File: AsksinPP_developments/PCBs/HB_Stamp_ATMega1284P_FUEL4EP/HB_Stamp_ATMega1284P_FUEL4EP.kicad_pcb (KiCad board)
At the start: 2 copper layers, 22 x 40 mm, 39 parts, among them J1 Power, J2 FTDI Debuger, J3 ISP Programmer, J4 I2C, J5 PA5/PCINT5, J6 PB3/AIN1/PCINT11, J7 PC4/PCINT20, U1 ATmega1284P-AU, U2 TPS61221DCK

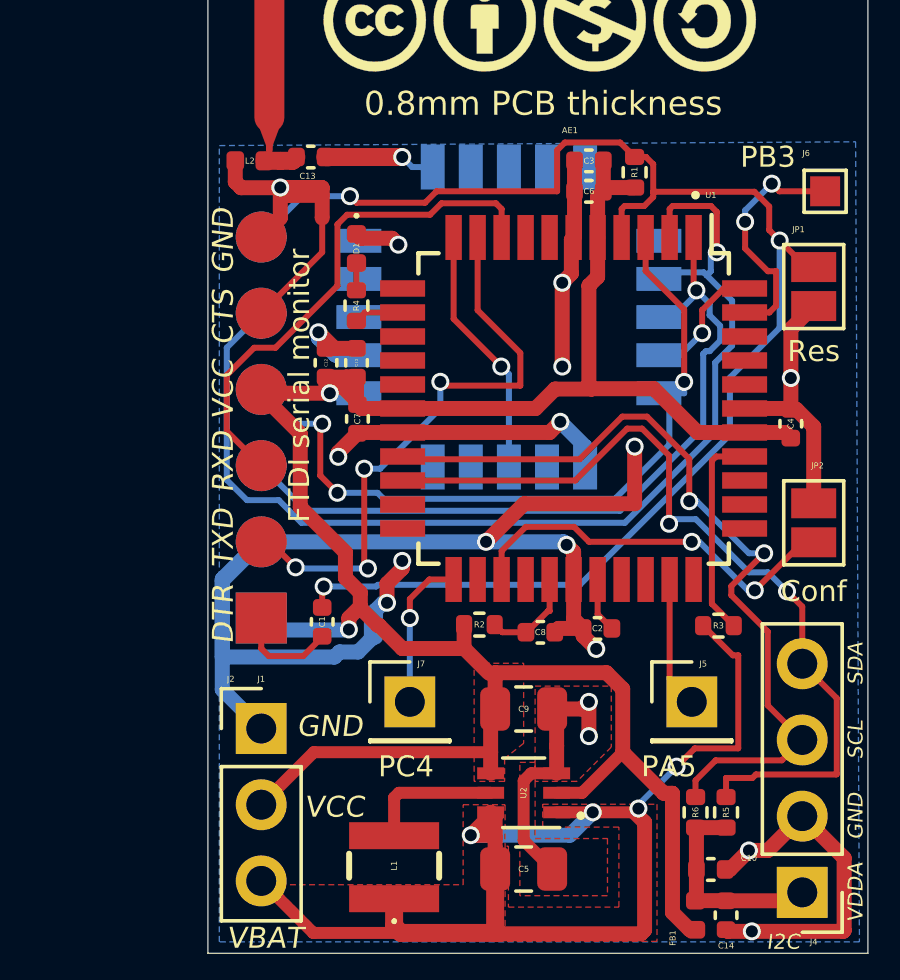
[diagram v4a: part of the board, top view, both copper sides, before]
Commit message: PCBs: HB_Stamp_ATMega1284P_FUEL4EP: Realized pads for pogo pin adapter as ring
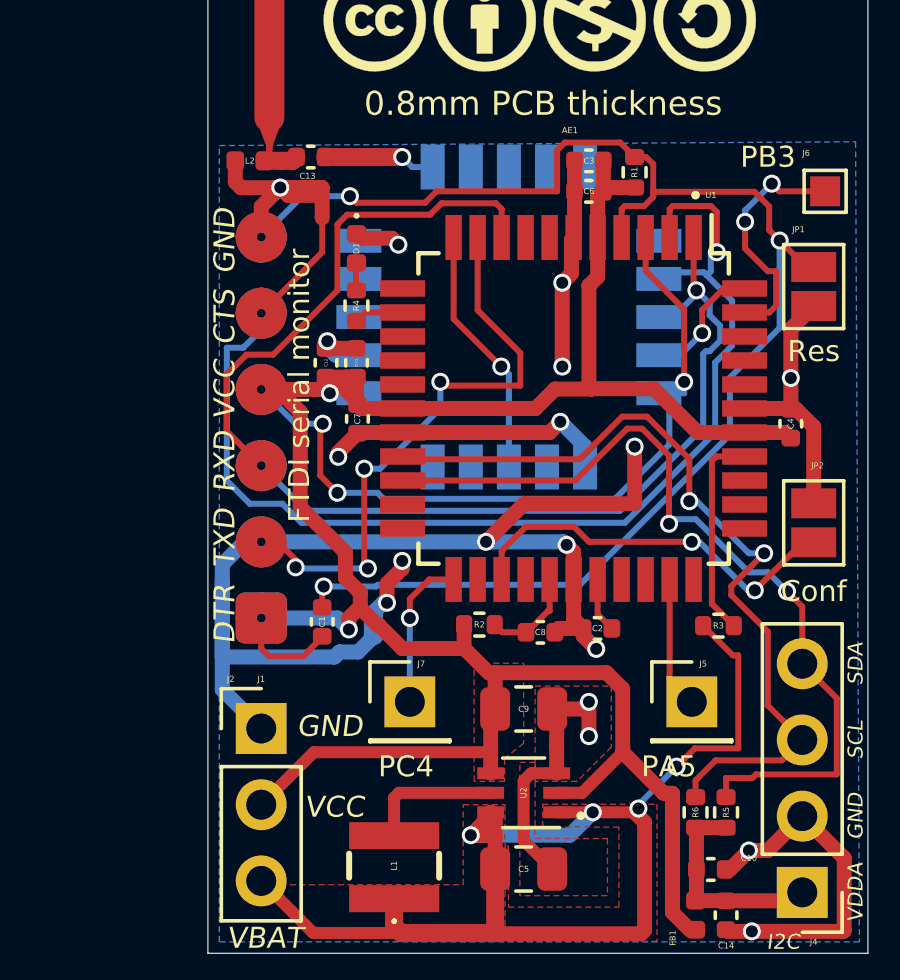
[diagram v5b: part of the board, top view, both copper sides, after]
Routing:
- net GND: track 102.8 -> 98.8 mm
- net VCC: track 78.3 -> 77.7 mm
- net /DTR: track 3.42 -> 2.87 mm
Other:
- board text added: "Version 1.4 - 02/2024 (KiCAD 6)"
- board text removed: "Version 1.3 - 02/2024 (KiCAD 6)"

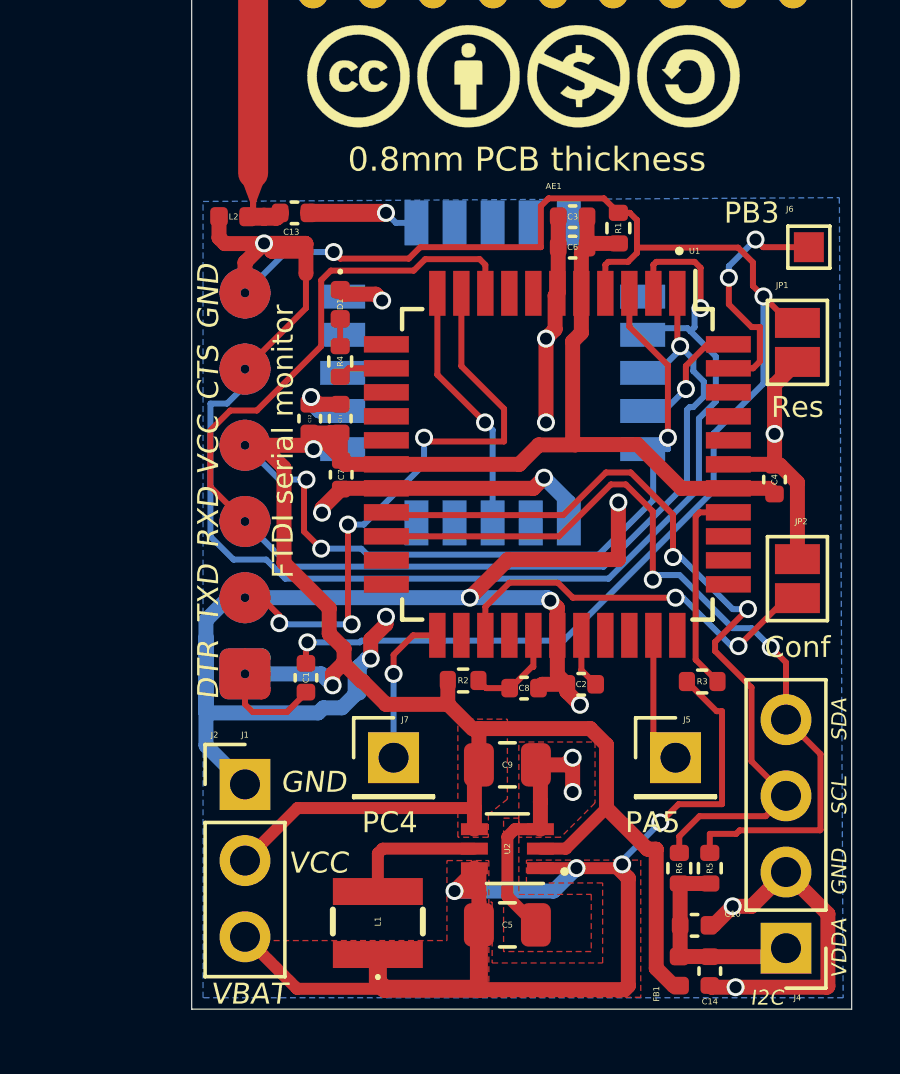
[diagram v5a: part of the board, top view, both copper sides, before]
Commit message: PCBs/HB_Stamp_ATMega1284P_FUEL4EP: migration to KiCAD 8
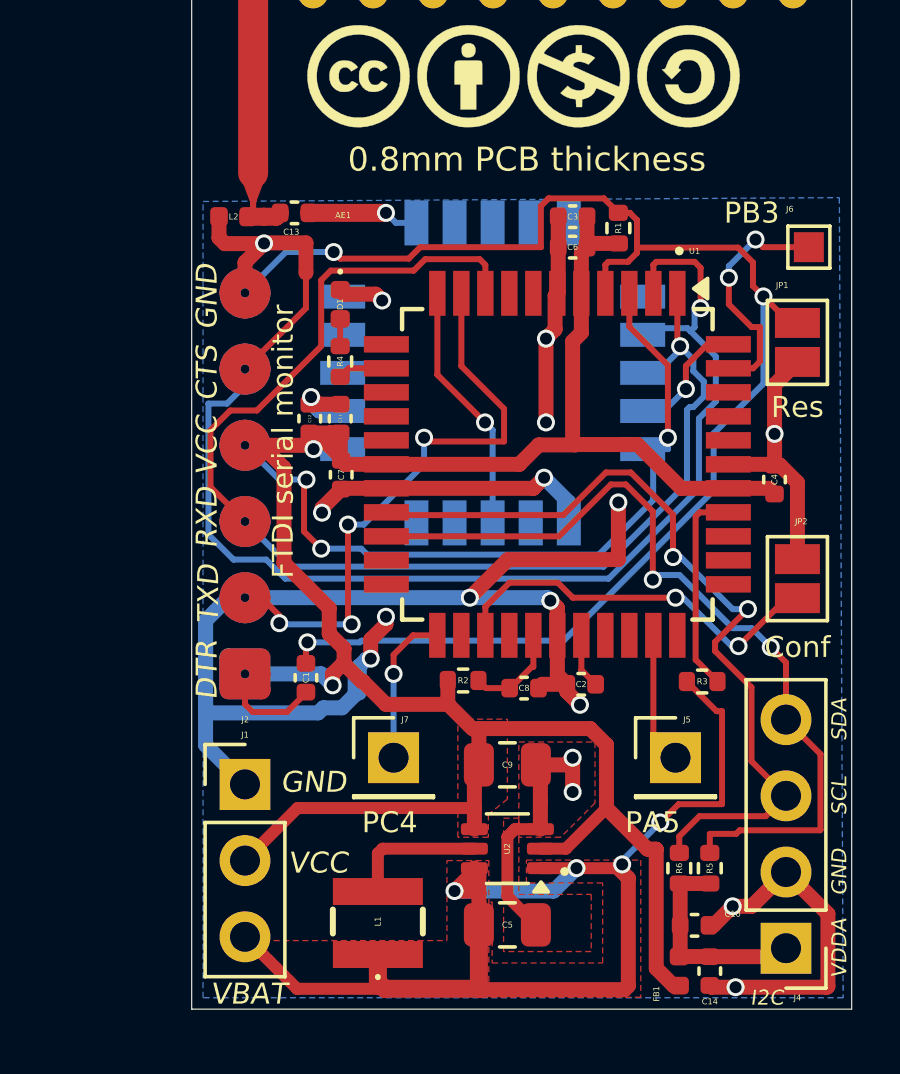
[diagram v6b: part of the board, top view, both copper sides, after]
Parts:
- AE1: footprint RF_Antenna:Texas_SWRA416_868MHz_915MHz -> FUEL4EP:Texas_SWRA416_868MHz_915MHz
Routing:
- net GND: track 98.8 -> 96.6 mm
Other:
- board text added: "868MHz SWRA416 antenna"
- board text added: "Version 1.5 - 09/2024 (KiCAD 8)"
- board text removed: "868MHz SWRA416 antrenna"
- board text removed: "Version 1.4 - 02/2024 (KiCAD 6)"

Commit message: PCBs: updated some JLCPCB manufacturing data after trial-order
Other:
- board text added: "JLCJLCJLCJLC"

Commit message: PCB updates
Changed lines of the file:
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@@
 		(attr smd)
 		(fp_line
-			(start -0.4 -1.5)
-			(end 0.4 -1.5)
+			(start -0.254 -1.524)
+			(end 0.254 -1.524)
 			(stroke
-				(width 0.2)
-				(type solid)
+				(width 0.12)
+				(type default)
 			)
 			(layer "F.SilkS")
@@
 		)
 		(fp_line
-			(start -0.4 1.5)
-			(end 0.4 1.5)
+			(start -0.254 1.524)
+			(end 0.254 1.524)
 			(stroke
-				(width 0.2)
-				(type solid)
+				(width 0.12)
+				(type default)
 			)
 			(layer "F.SilkS")
@@
 			)
 		)
-		(fp_text user "KEEP-OUT ZONE"
-			(at 1 -2.8 0)
+		(fp_text user "No metal, traces or "
+			(at 1 0.2 0)
 			(layer "Cmts.User")
 			(effects
@@
 			)
 		)
-		(fp_text user "No metal, traces or "
-			(at 1 0.2 0)
+		(fp_text user "KEEP-OUT ZONE"
+			(at 1 -2.8 0)
 			(layer "Cmts.User")
 			(effects
@@
 		(sheetfile "HB_Stamp_ATMega1284P_FUEL4EP.kicad_sch")
 		(zone_connect 1)
-		(attr exclude_from_pos_files exclude_from_bom)
+		(attr exclude_from_pos_files)
 		(fp_line
 			(start 1.4 -1)
@@
 		(sheetfile "HB_Stamp_ATMega1284P_FUEL4EP.kicad_sch")
 		(zone_connect 1)
-		(attr exclude_from_pos_files exclude_from_bom)
+		(attr exclude_from_pos_files)
 		(fp_line
 			(start 1.4 -1)
@@
 			)
 		)
-		(property "LCSC" "C3223181"
+		(property "LCSC" "C2043991"
 			(at 2.794 -52.832 0)
 			(layer "F.Fab")
@@
 			)
 		)
-		(property "Sim.Enable" ""
-			(at 0 0 180)
-			(unlocked yes)
-			(layer "F.Fab")
-			(hide yes)
-			(effects
-				(font
-					(size 1 1)
-					(thickness 0.15)
-				)
-			)
-		)
 		(property ki_fp_filters "Choke_* *Coil* Inductor_* L_*")
 		(sheetname "Stammblatt")
@@
 		(attr smd exclude_from_pos_files)
 		(fp_line
-			(start 0 -10)
-			(end 0 -8.02)
+			(start 0 -10.033)
+			(end 0 -8.255)
 			(stroke
 				(width 0.12)
-				(type solid)
+				(type default)
 			)
 			(layer "B.SilkS")
 		)
 		(fp_line
-			(start 0 -8.02)
-			(end 0.9 -8.02)
+			(start 0 -10.033)
+			(end 1.651 -10.033)
 			(stroke
 				(width 0.12)
-				(type solid)
+				(type default)
 			)
 			(layer "B.SilkS")
 		)
 		(fp_line
-			(start 0 -1.96)
-			(end 0 0)
+			(start 0 -8.255)
+			(end 1.016 -8.255)
 			(stroke
 				(width 0.12)
-				(type solid)
+				(type default)
 			)
 			(layer "B.SilkS")
@@
 		(fp_line
 			(start 0 0)
-			(end 1.98 0)
+			(end 0 -1.778)
 			(stroke
 				(width 0.12)
-				(type solid)
+				(type default)
 			)
 			(layer "B.SilkS")
 		)
 		(fp_line
-			(start 0.9 -8.02)
-			(end 0.9 -1.96)
+			(start 0 0)
+			(end 1.651 0)
 			(stroke
 				(width 0.12)
-				(type solid)
+				(type default)
 			)
 			(layer "B.SilkS")
 		)
 		(fp_line
-			(start 0.9 -1.96)
-			(end 0 -1.96)
+			(start 1.016 -8.255)
+			(end 1.016 -8.128)
 			(stroke
 				(width 0.12)
-				(type solid)
+				(type default)
+			)
+			(layer "B.SilkS")
+		)
+		(fp_line
+			(start 1.016 -8.128)
+			(end 1.016 -1.778)
+			(stroke
+				(width 0.12)
+				(type default)
+			)
+			(layer "B.SilkS")
+		)
+		(fp_line
+			(start 1.016 -1.778)
+			(end 0 -1.778)
+			(stroke
+				(width 0.12)
+				(type default)
 			)
 			(layer "B.SilkS")
@@
 		)
 		(fp_line
-			(start 1.96 -10)
-			(end 0 -10)
+			(start 1.651 -10.033)
+			(end 1.651 -9.017)
 			(stroke
 				(width 0.12)
-				(type solid)
+				(type default)
 			)
 			(layer "B.SilkS")
 		)
 		(fp_line
-			(start 1.96 -9.1)
-			(end 1.96 -10)
+			(start 1.651 -9.017)
+			(end 1.778 -9.017)
 			(stroke
 				(width 0.12)
-				(type solid)
+				(type default)
 			)
 			(layer "B.SilkS")
 		)
 		(fp_line
-			(start 1.98 -0.9)
-			(end 8.04 -0.9)
+			(start 1.651 -1.016)
+			(end 1.778 -1.016)
 			(stroke
 				(width 0.12)
-				(type solid)
+				(type default)
 			)
 			(layer "B.SilkS")
 		)
 		(fp_line
-			(start 1.98 0)
-			(end 1.98 -0.9)
+			(start 1.651 0)
+			(end 1.651 -1.016)
 			(stroke
 				(width 0.12)
-				(type solid)
+				(type default)
 			)
 			(layer "B.SilkS")
 		)
 		(fp_line
-			(start 8.02 -10)
-			(end 8.02 -9.1)
+			(start 1.778 -1.016)
+			(end 1.905 -1.016)
 			(stroke
 				(width 0.12)
-				(type solid)
+				(type default)
 			)
 			(layer "B.SilkS")
 		)
 		(fp_line
-			(start 8.02 -9.1)
-			(end 1.96 -9.1)
+			(start 1.905 -1.016)
+			(end 8.128 -1.016)
 			(stroke
 				(width 0.12)
-				(type solid)
+				(type default)
 			)
 			(layer "B.SilkS")
 		)
 		(fp_line
-			(start 8.04 -0.9)
-			(end 8.04 0)
+			(start 8.255 -9.017)
+			(end 1.778 -9.017)
 			(stroke
 				(width 0.12)
-				(type solid)
+				(type default)
 			)
 			(layer "B.SilkS")
 		)
 		(fp_line
-			(start 8.04 0)
-			(end 10 0)
+			(start 8.255 -9.017)
+			(end 8.255 -10.033)
 			(stroke
 				(width 0.12)
-				(type solid)
+				(type default)
+			)
+			(layer "B.SilkS")
+		)
+		(fp_line
+			(start 8.255 -1.016)
+			(end 8.128 -1.016)
+			(stroke
+				(width 0.12)
+				(type default)
+			)
+			(layer "B.SilkS")
+		)
+		(fp_line
+			(start 8.255 0)
+			(end 8.255 -1.016)
+			(stroke
+				(width 0.12)
+				(type default)
 			)
 			(layer "B.SilkS")
@@
 		)
 		(fp_line
-			(start 9.1 -8.04)
-			(end 10 -8.04)
+			(start 9.017 -8.255)
+			(end 9.017 -8.128)
 			(stroke
 				(width 0.12)
-				(type solid)
+				(type default)
 			)
 			(layer "B.SilkS")
 		)
 		(fp_line
-			(start 9.1 -1.98)
-			(end 9.1 -8.04)
+			(start 9.017 -1.778)
+			(end 9.017 -8.128)
 			(stroke
 				(width 0.12)
-				(type solid)
+				(type default)
 			)
 			(layer "B.SilkS")
 		)
 		(fp_line
-			(start 10 -10)
-			(end 8.02 -10)
+			(start 9.017 -1.778)
+			(end 10.033 -1.778)
 			(stroke
 				(width 0.12)
-				(type solid)
+				(type default)
 			)
 			(layer "B.SilkS")
 		)
 		(fp_line
-			(start 10 -8.04)
-			(end 10 -10)
+			(start 10 -10.033)
+			(end 8.255 -10.033)
 			(stroke
 				(width 0.12)
-				(type solid)
+				(type default)
 			)
 			(layer "B.SilkS")
 		)
 		(fp_line
-			(start 10 -1.98)
-			(end 9.1 -1.98)
+			(start 10.033 -10.033)
+			(end 10.033 -8.255)
 			(stroke
 				(width 0.12)
-				(type solid)
+				(type default)
 			)
 			(layer "B.SilkS")
 		)
 		(fp_line
-			(start 10 0)
-			(end 10 -1.98)
+			(start 10.033 -8.255)
+			(end 9.017 -8.255)
 			(stroke
 				(width 0.12)
-				(type solid)
+				(type default)
+			)
+			(layer "B.SilkS")
+		)
+		(fp_line
+			(start 10.033 0)
+			(end 8.255 0)
+			(stroke
+				(width 0.12)
+				(type default)
+			)
+			(layer "B.SilkS")
+		)
+		(fp_line
+			(start 10.033 0)
+			(end 10.033 -1.778)
+			(stroke
+				(width 0.12)
+				(type default)
 			)
 			(layer "B.SilkS")
@@
 			(layer "B.CrtYd")
 		)
-		(fp_text user "eByte E07-900MM10S"
-			(at 11.604 -5 90)
+		(fp_text user "16"
+			(at 7.55 -1.8 180)
+			(unlocked yes)
 			(layer "B.SilkS")
 			(effects
 				(font
-					(size 0.7 0.7)
-					(thickness 0.1)
+					(size 0.2 0.2)
+					(thickness 0.125)
 				)
 				(justify mirror)
@@
 			)
 		)
-		(fp_text user "1"
-			(at 1.55 -2.5 180)
-			(unlocked yes)
+		(fp_text user "eByte E07-900MM10S"
+			(at 11.604 -5 90)
 			(layer "B.SilkS")
 			(effects
 				(font
-					(size 0.2 0.2)
-					(thickness 0.125)
+					(size 0.7 0.7)
+					(thickness 0.1)
 				)
 				(justify mirror)
 			)
 		)
-		(fp_text user "16"
-			(at 7.55 -1.8 180)
+		(fp_text user "1"
+			(at 1.55 -2.5 180)
 			(unlocked yes)
 			(layer "B.SilkS")
@@
 			(primitives
 				(gr_rect
-					(start -1.1 -0.55)
-					(end 0 0.55)
+					(start -1.1 0.55)
+					(end 0 -0.55)
 					(width 0.6)
 					(fill no)
